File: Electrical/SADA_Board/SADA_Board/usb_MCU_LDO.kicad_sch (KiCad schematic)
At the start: 12 parts

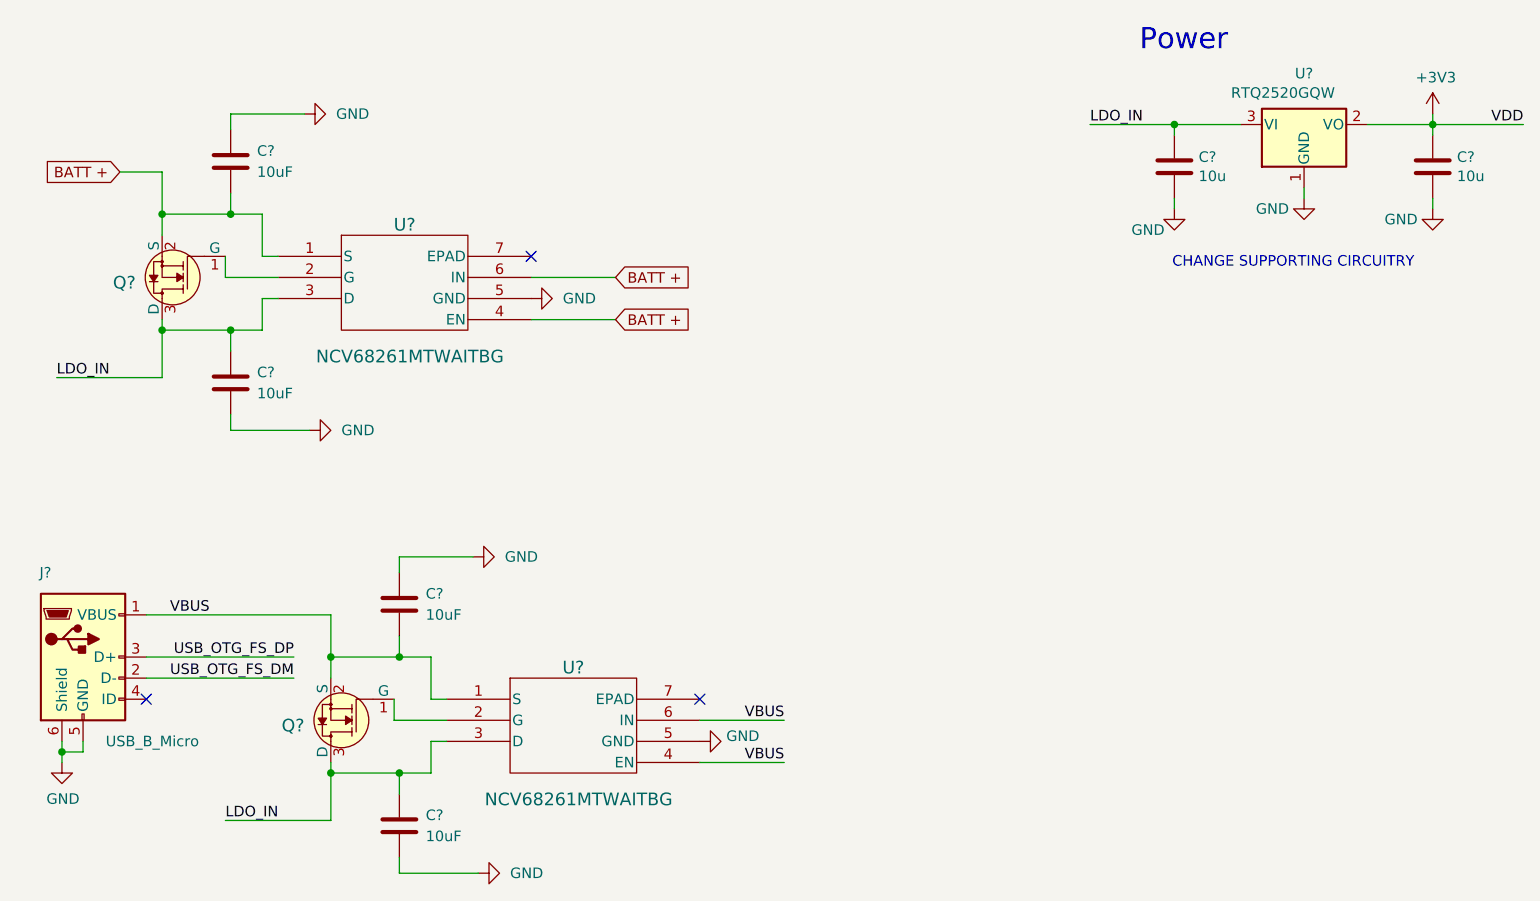
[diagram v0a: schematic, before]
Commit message: Partial implementation of stepper motor Step up
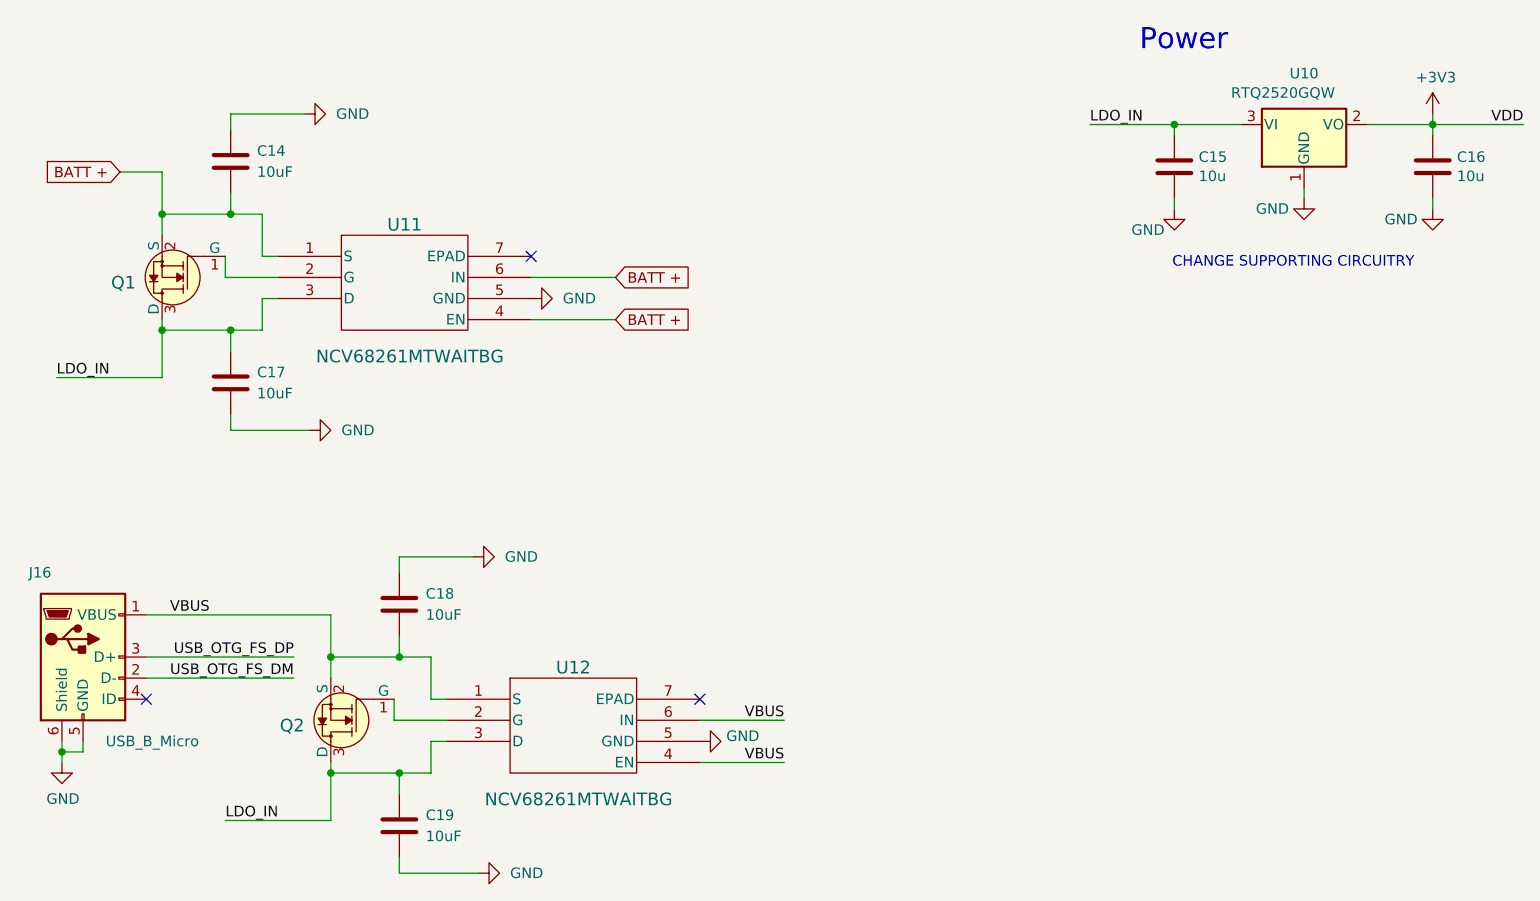
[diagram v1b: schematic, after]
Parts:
- gave numbers to parts that had none: 12
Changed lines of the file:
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@@
   (symbol (lib_id "Ideal_diode_NCV:NCV68261MTWAITBG") (at 74.93 111.76 0) (unit 1)
     (in_bom yes) (on_board yes)
-    (property "Reference" "U?" (id 0) (at 74.93 105.41 0)
+    (property "Reference" "U11" (id 0) (at 74.93 105.41 0)
       (effects (font (size 1.524 1.524)))
     )
@@
   (symbol (lib_id "power:GND") (at 83.82 183.515 90) (unit 1)
     (in_bom yes) (on_board yes) (fields_autoplaced)
-    (property "Reference" "#PWR?" (id 0) (at 90.17 183.515 0)
+    (property "Reference" "#PWR058" (id 0) (at 90.17 183.515 0)
       (effects (font (size 1.27 1.27)) hide)
     )
@@
   (symbol (lib_id "Device:C") (at 74.295 177.8 0) (unit 1)
     (in_bom yes) (on_board yes) (fields_autoplaced)
-    (property "Reference" "C?" (id 0) (at 77.47 176.5299 0)
+    (property "Reference" "C19" (id 0) (at 77.47 176.5299 0)
       (effects (font (size 1.27 1.27)) (justify left))
     )
@@
   (symbol (lib_id "power:GND") (at 167.64 103.505 0) (unit 1)
     (in_bom yes) (on_board yes)
-    (property "Reference" "#PWR?" (id 0) (at 167.64 109.855 0)
+    (property "Reference" "#PWR051" (id 0) (at 167.64 109.855 0)
       (effects (font (size 1.27 1.27)) hide)
     )
@@
   (symbol (lib_id "Device:C") (at 74.295 151.13 0) (unit 1)
     (in_bom yes) (on_board yes) (fields_autoplaced)
-    (property "Reference" "C?" (id 0) (at 77.47 149.8599 0)
+    (property "Reference" "C18" (id 0) (at 77.47 149.8599 0)
       (effects (font (size 1.27 1.27)) (justify left))
     )
@@
   (symbol (lib_id "Regulator_Linear:NCP1117-3.3_SOT223") (at 183.261 93.345 0) (unit 1)
     (in_bom yes) (on_board yes)
-    (property "Reference" "U?" (id 0) (at 183.261 87.1982 0))
+    (property "Reference" "U10" (id 0) (at 183.261 87.1982 0))
     (property "Value" "RTQ2520GQW" (id 1) (at 180.721 89.535 0))
     (property "Footprint" "" (id 2) (at 183.261 88.265 0)
@@
   (symbol (lib_id "power:GND") (at 90.17 114.3 90) (unit 1)
     (in_bom yes) (on_board yes) (fields_autoplaced)
-    (property "Reference" "#PWR?" (id 0) (at 96.52 114.3 0)
+    (property "Reference" "#PWR053" (id 0) (at 96.52 114.3 0)
       (effects (font (size 1.27 1.27)) hide)
     )
@@
   (symbol (lib_id "power:GND") (at 62.865 92.075 90) (unit 1)
     (in_bom yes) (on_board yes) (fields_autoplaced)
-    (property "Reference" "#PWR?" (id 0) (at 69.215 92.075 0)
+    (property "Reference" "#PWR048" (id 0) (at 69.215 92.075 0)
       (effects (font (size 1.27 1.27)) hide)
     )
@@
   (symbol (lib_id "dk_Transistors-FETs-MOSFETs-Single:2N7002") (at 45.72 111.76 180) (unit 1)
     (in_bom yes) (on_board yes) (fields_autoplaced)
-    (property "Reference" "Q?" (id 0) (at 42.545 112.395 0)
+    (property "Reference" "Q1" (id 0) (at 42.545 112.395 0)
       (effects (font (size 1.524 1.524)) (justify left))
     )
@@
   (symbol (lib_id "Device:C") (at 53.975 97.79 0) (unit 1)
     (in_bom yes) (on_board yes) (fields_autoplaced)
-    (property "Reference" "C?" (id 0) (at 57.15 96.5199 0)
+    (property "Reference" "C14" (id 0) (at 57.15 96.5199 0)
       (effects (font (size 1.27 1.27)) (justify left))
     )
@@
   (symbol (lib_id "power:GND") (at 33.655 170.18 0) (unit 1)
     (in_bom yes) (on_board yes)
-    (property "Reference" "#PWR?" (id 0) (at 33.655 176.53 0)
+    (property "Reference" "#PWR057" (id 0) (at 33.655 176.53 0)
       (effects (font (size 1.27 1.27)) hide)
     )
@@
   (symbol (lib_id "power:GND") (at 83.185 145.415 90) (unit 1)
     (in_bom yes) (on_board yes) (fields_autoplaced)
-    (property "Reference" "#PWR?" (id 0) (at 89.535 145.415 0)
+    (property "Reference" "#PWR055" (id 0) (at 89.535 145.415 0)
       (effects (font (size 1.27 1.27)) hide)
     )
@@
   (symbol (lib_id "power:+3V3") (at 198.755 92.075 0) (unit 1)
     (in_bom yes) (on_board yes)
-    (property "Reference" "#PWR?" (id 0) (at 198.755 95.885 0)
+    (property "Reference" "#PWR049" (id 0) (at 198.755 95.885 0)
       (effects (font (size 1.27 1.27)) hide)
     )
@@
   (symbol (lib_id "Device:C") (at 53.975 124.46 0) (unit 1)
     (in_bom yes) (on_board yes) (fields_autoplaced)
-    (property "Reference" "C?" (id 0) (at 57.15 123.1899 0)
+    (property "Reference" "C17" (id 0) (at 57.15 123.1899 0)
       (effects (font (size 1.27 1.27)) (justify left))
     )
@@
   (symbol (lib_id "dk_Transistors-FETs-MOSFETs-Single:2N7002") (at 66.04 165.1 180) (unit 1)
     (in_bom yes) (on_board yes) (fields_autoplaced)
-    (property "Reference" "Q?" (id 0) (at 62.865 165.735 0)
+    (property "Reference" "Q2" (id 0) (at 62.865 165.735 0)
       (effects (font (size 1.524 1.524)) (justify left))
     )
@@
   (symbol (lib_id "power:GND") (at 63.5 130.175 90) (unit 1)
     (in_bom yes) (on_board yes) (fields_autoplaced)
-    (property "Reference" "#PWR?" (id 0) (at 69.85 130.175 0)
+    (property "Reference" "#PWR054" (id 0) (at 69.85 130.175 0)
       (effects (font (size 1.27 1.27)) hide)
     )
@@
   (symbol (lib_id "power:GND") (at 110.49 167.64 90) (unit 1)
     (in_bom yes) (on_board yes)
-    (property "Reference" "#PWR?" (id 0) (at 116.84 167.64 0)
+    (property "Reference" "#PWR056" (id 0) (at 116.84 167.64 0)
       (effects (font (size 1.27 1.27)) hide)
     )
@@
   (symbol (lib_id "power:GND") (at 183.261 102.235 0) (unit 1)
     (in_bom yes) (on_board yes)
-    (property "Reference" "#PWR?" (id 0) (at 183.261 108.585 0)
+    (property "Reference" "#PWR050" (id 0) (at 183.261 108.585 0)
       (effects (font (size 1.27 1.27)) hide)
     )
@@
   (symbol (lib_id "RP2040_minimal-rescue:USB_B_Micro-Connector") (at 36.195 157.48 0) (unit 1)
     (in_bom yes) (on_board yes)
-    (property "Reference" "J?" (id 0) (at 32.385 147.32 0)
+    (property "Reference" "J16" (id 0) (at 32.385 147.32 0)
       (effects (font (size 1.27 1.27)) (justify right))
     )
@@
   (symbol (lib_id "Ideal_diode_NCV:NCV68261MTWAITBG") (at 95.25 165.1 0) (unit 1)
     (in_bom yes) (on_board yes)
-    (property "Reference" "U?" (id 0) (at 95.25 158.75 0)
+    (property "Reference" "U12" (id 0) (at 95.25 158.75 0)
       (effects (font (size 1.524 1.524)))
     )
@@
   (symbol (lib_id "Device:C") (at 198.755 98.425 0) (unit 1)
     (in_bom yes) (on_board yes)
-    (property "Reference" "C?" (id 0) (at 201.676 97.2566 0)
+    (property "Reference" "C16" (id 0) (at 201.676 97.2566 0)
       (effects (font (size 1.27 1.27)) (justify left))
     )
@@
   (symbol (lib_id "Device:C") (at 167.64 98.425 0) (unit 1)
     (in_bom yes) (on_board yes)
-    (property "Reference" "C?" (id 0) (at 170.561 97.2566 0)
+    (property "Reference" "C15" (id 0) (at 170.561 97.2566 0)
       (effects (font (size 1.27 1.27)) (justify left))
     )
@@
   (symbol (lib_id "power:GND") (at 198.755 103.505 0) (unit 1)
     (in_bom yes) (on_board yes)
-    (property "Reference" "#PWR?" (id 0) (at 198.755 109.855 0)
-      (effects (font (size 1.27 1.27)) hide)
-    )
+    (property "Reference" "#PWR052" (id 0) (at 198.755 109.855 0)
+      (effects (font (size 1.27 1.27)) hide)
+    )

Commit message: Rough draft stepup done
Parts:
- renumbered C14 to C23, C15 to C24, C16 to C25, C17 to C26, C18 to C27, C19 to C28, Q1 to Q2, Q2 to Q3, U10 to U11, U11 to U12, U12 to U13
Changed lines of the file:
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@@
   (symbol (lib_id "Ideal_diode_NCV:NCV68261MTWAITBG") (at 74.93 111.76 0) (unit 1)
     (in_bom yes) (on_board yes)
-    (property "Reference" "U11" (id 0) (at 74.93 105.41 0)
+    (property "Reference" "U12" (id 0) (at 74.93 105.41 0)
       (effects (font (size 1.524 1.524)))
     )
@@
   (symbol (lib_id "power:GND") (at 83.82 183.515 90) (unit 1)
     (in_bom yes) (on_board yes) (fields_autoplaced)
-    (property "Reference" "#PWR058" (id 0) (at 90.17 183.515 0)
+    (property "Reference" "#PWR072" (id 0) (at 90.17 183.515 0)
       (effects (font (size 1.27 1.27)) hide)
     )
@@
   (symbol (lib_id "Device:C") (at 74.295 177.8 0) (unit 1)
     (in_bom yes) (on_board yes) (fields_autoplaced)
-    (property "Reference" "C19" (id 0) (at 77.47 176.5299 0)
+    (property "Reference" "C28" (id 0) (at 77.47 176.5299 0)
       (effects (font (size 1.27 1.27)) (justify left))
     )
@@
   (symbol (lib_id "power:GND") (at 167.64 103.505 0) (unit 1)
     (in_bom yes) (on_board yes)
-    (property "Reference" "#PWR051" (id 0) (at 167.64 109.855 0)
+    (property "Reference" "#PWR065" (id 0) (at 167.64 109.855 0)
       (effects (font (size 1.27 1.27)) hide)
     )
@@
   (symbol (lib_id "Device:C") (at 74.295 151.13 0) (unit 1)
     (in_bom yes) (on_board yes) (fields_autoplaced)
-    (property "Reference" "C18" (id 0) (at 77.47 149.8599 0)
+    (property "Reference" "C27" (id 0) (at 77.47 149.8599 0)
       (effects (font (size 1.27 1.27)) (justify left))
     )
@@
   (symbol (lib_id "Regulator_Linear:NCP1117-3.3_SOT223") (at 183.261 93.345 0) (unit 1)
     (in_bom yes) (on_board yes)
-    (property "Reference" "U10" (id 0) (at 183.261 87.1982 0))
+    (property "Reference" "U11" (id 0) (at 183.261 87.1982 0))
     (property "Value" "RTQ2520GQW" (id 1) (at 180.721 89.535 0))
     (property "Footprint" "" (id 2) (at 183.261 88.265 0)
@@
   (symbol (lib_id "power:GND") (at 90.17 114.3 90) (unit 1)
     (in_bom yes) (on_board yes) (fields_autoplaced)
-    (property "Reference" "#PWR053" (id 0) (at 96.52 114.3 0)
+    (property "Reference" "#PWR067" (id 0) (at 96.52 114.3 0)
       (effects (font (size 1.27 1.27)) hide)
     )
@@
   (symbol (lib_id "power:GND") (at 62.865 92.075 90) (unit 1)
     (in_bom yes) (on_board yes) (fields_autoplaced)
-    (property "Reference" "#PWR048" (id 0) (at 69.215 92.075 0)
+    (property "Reference" "#PWR062" (id 0) (at 69.215 92.075 0)
       (effects (font (size 1.27 1.27)) hide)
     )
@@
   (symbol (lib_id "dk_Transistors-FETs-MOSFETs-Single:2N7002") (at 45.72 111.76 180) (unit 1)
     (in_bom yes) (on_board yes) (fields_autoplaced)
-    (property "Reference" "Q1" (id 0) (at 42.545 112.395 0)
+    (property "Reference" "Q2" (id 0) (at 42.545 112.395 0)
       (effects (font (size 1.524 1.524)) (justify left))
     )
@@
   (symbol (lib_id "Device:C") (at 53.975 97.79 0) (unit 1)
     (in_bom yes) (on_board yes) (fields_autoplaced)
-    (property "Reference" "C14" (id 0) (at 57.15 96.5199 0)
+    (property "Reference" "C23" (id 0) (at 57.15 96.5199 0)
       (effects (font (size 1.27 1.27)) (justify left))
     )
@@
   (symbol (lib_id "power:GND") (at 33.655 170.18 0) (unit 1)
     (in_bom yes) (on_board yes)
-    (property "Reference" "#PWR057" (id 0) (at 33.655 176.53 0)
+    (property "Reference" "#PWR071" (id 0) (at 33.655 176.53 0)
       (effects (font (size 1.27 1.27)) hide)
     )
@@
   (symbol (lib_id "power:GND") (at 83.185 145.415 90) (unit 1)
     (in_bom yes) (on_board yes) (fields_autoplaced)
-    (property "Reference" "#PWR055" (id 0) (at 89.535 145.415 0)
+    (property "Reference" "#PWR069" (id 0) (at 89.535 145.415 0)
       (effects (font (size 1.27 1.27)) hide)
     )
@@
   (symbol (lib_id "power:+3V3") (at 198.755 92.075 0) (unit 1)
     (in_bom yes) (on_board yes)
-    (property "Reference" "#PWR049" (id 0) (at 198.755 95.885 0)
+    (property "Reference" "#PWR063" (id 0) (at 198.755 95.885 0)
       (effects (font (size 1.27 1.27)) hide)
     )
@@
   (symbol (lib_id "Device:C") (at 53.975 124.46 0) (unit 1)
     (in_bom yes) (on_board yes) (fields_autoplaced)
-    (property "Reference" "C17" (id 0) (at 57.15 123.1899 0)
+    (property "Reference" "C26" (id 0) (at 57.15 123.1899 0)
       (effects (font (size 1.27 1.27)) (justify left))
     )
@@
   (symbol (lib_id "dk_Transistors-FETs-MOSFETs-Single:2N7002") (at 66.04 165.1 180) (unit 1)
     (in_bom yes) (on_board yes) (fields_autoplaced)
-    (property "Reference" "Q2" (id 0) (at 62.865 165.735 0)
+    (property "Reference" "Q3" (id 0) (at 62.865 165.735 0)
       (effects (font (size 1.524 1.524)) (justify left))
     )
@@
   (symbol (lib_id "power:GND") (at 63.5 130.175 90) (unit 1)
     (in_bom yes) (on_board yes) (fields_autoplaced)
-    (property "Reference" "#PWR054" (id 0) (at 69.85 130.175 0)
+    (property "Reference" "#PWR068" (id 0) (at 69.85 130.175 0)
       (effects (font (size 1.27 1.27)) hide)
     )
@@
   (symbol (lib_id "power:GND") (at 110.49 167.64 90) (unit 1)
     (in_bom yes) (on_board yes)
-    (property "Reference" "#PWR056" (id 0) (at 116.84 167.64 0)
+    (property "Reference" "#PWR070" (id 0) (at 116.84 167.64 0)
       (effects (font (size 1.27 1.27)) hide)
     )
@@
   (symbol (lib_id "power:GND") (at 183.261 102.235 0) (unit 1)
     (in_bom yes) (on_board yes)
-    (property "Reference" "#PWR050" (id 0) (at 183.261 108.585 0)
+    (property "Reference" "#PWR064" (id 0) (at 183.261 108.585 0)
       (effects (font (size 1.27 1.27)) hide)
     )
@@
   (symbol (lib_id "Ideal_diode_NCV:NCV68261MTWAITBG") (at 95.25 165.1 0) (unit 1)
     (in_bom yes) (on_board yes)
-    (property "Reference" "U12" (id 0) (at 95.25 158.75 0)
+    (property "Reference" "U13" (id 0) (at 95.25 158.75 0)
       (effects (font (size 1.524 1.524)))
     )
@@
   (symbol (lib_id "Device:C") (at 198.755 98.425 0) (unit 1)
     (in_bom yes) (on_board yes)
-    (property "Reference" "C16" (id 0) (at 201.676 97.2566 0)
+    (property "Reference" "C25" (id 0) (at 201.676 97.2566 0)
       (effects (font (size 1.27 1.27)) (justify left))
     )
@@
   (symbol (lib_id "Device:C") (at 167.64 98.425 0) (unit 1)
     (in_bom yes) (on_board yes)
-    (property "Reference" "C15" (id 0) (at 170.561 97.2566 0)
+    (property "Reference" "C24" (id 0) (at 170.561 97.2566 0)
       (effects (font (size 1.27 1.27)) (justify left))
     )
@@
   (symbol (lib_id "power:GND") (at 198.755 103.505 0) (unit 1)
     (in_bom yes) (on_board yes)
-    (property "Reference" "#PWR052" (id 0) (at 198.755 109.855 0)
-      (effects (font (size 1.27 1.27)) hide)
-    )
+    (property "Reference" "#PWR066" (id 0) (at 198.755 109.855 0)
+      (effects (font (size 1.27 1.27)) hide)
+    )
